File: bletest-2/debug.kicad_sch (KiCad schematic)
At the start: 2 parts, among them J3 Conn_ARM_JTAG_SWD_10

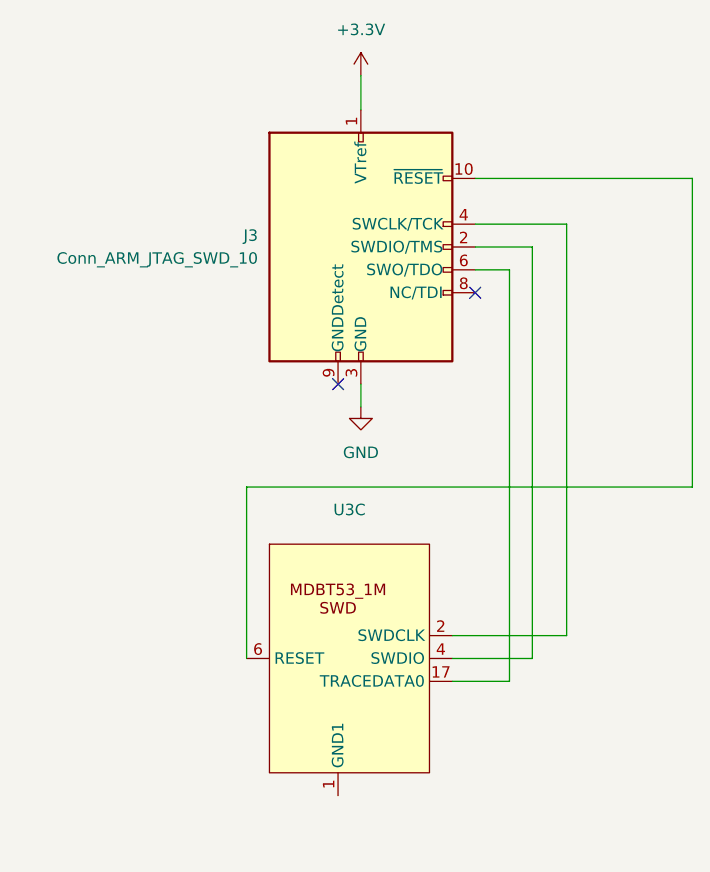
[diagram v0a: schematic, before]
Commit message: Full routing done
There are still a bunch of ERC violations.
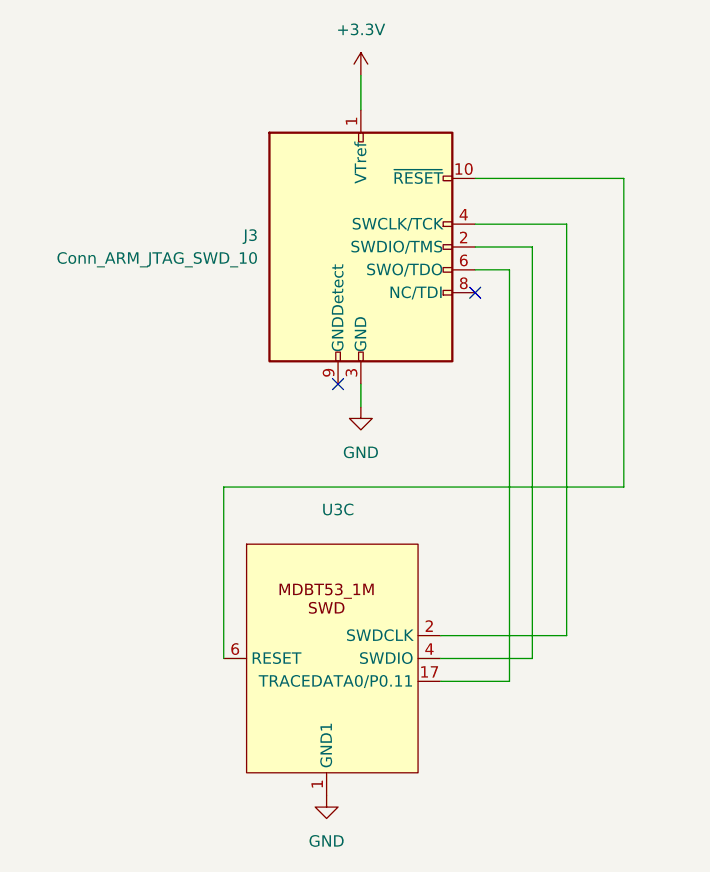
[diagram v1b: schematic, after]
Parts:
- J3: symbol Connector:Conn_ARM_JTAG_SWD_10 -> David Brown Keyboard Parts:Conn_ARM_JTAG_SWD_10
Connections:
- net GND: now also U3.1 (GND1)
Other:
- moved on the sheet: U3C
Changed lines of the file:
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@@
 	(wire
 		(pts
-			(xy 106.68 93.98) (xy 106.68 59.69)
+			(xy 99.06 93.98) (xy 99.06 59.69)
 		)
 		(stroke
@@
 	(wire
 		(pts
-			(xy 88.9 113.03) (xy 80.01 113.03)
+			(xy 88.9 113.03) (xy 78.74 113.03)
 		)
 		(stroke
@@
 	(wire
 		(pts
-			(xy 92.71 110.49) (xy 80.01 110.49)
+			(xy 92.71 110.49) (xy 78.74 110.49)
 		)
 		(stroke
@@
 	(wire
 		(pts
-			(xy 57.15 113.03) (xy 57.15 93.98)
+			(xy 54.61 113.03) (xy 54.61 93.98)
 		)
 		(stroke
@@
 	(wire
 		(pts
-			(xy 106.68 59.69) (xy 82.55 59.69)
+			(xy 99.06 59.69) (xy 82.55 59.69)
 		)
 		(stroke
@@
 	(wire
 		(pts
-			(xy 57.15 93.98) (xy 106.68 93.98)
+			(xy 54.61 93.98) (xy 99.06 93.98)
 		)
 		(stroke
@@
 	(wire
 		(pts
-			(xy 86.36 115.57) (xy 80.01 115.57)
+			(xy 86.36 115.57) (xy 78.74 115.57)
 		)
 		(stroke
@@
 	(symbol
 		(lib_id "David Brown Keyboard Parts:MDBT53_1M")
-		(at 67.31 113.03 0)
+		(at 66.04 113.03 0)
 		(unit 3)
 		(exclude_from_sim no)
@@
 		(fields_autoplaced yes)
 		(property "Reference" "U3"
-			(at 68.58 96.52 0)
+			(at 67.31 96.52 0)
 			(effects
 				(font
@@
 		)
 		(property "Value" "~"
-			(at 68.58 99.06 0)
+			(at 67.31 99.06 0)
 			(effects
 				(font
@@
 		)
 		(property "Footprint" "davidb-keyboard-foot:MDBT53_1M"
-			(at 67.31 115.57 0)
+			(at 66.04 115.57 0)
 			(effects
 				(font
@@
 		)
 		(property "Datasheet" ""
-			(at 67.31 115.57 0)
+			(at 66.04 115.57 0)
 			(effects
 				(font
@@
 		)
 		(property "Description" ""
-			(at 67.31 115.57 0)
+			(at 66.04 115.57 0)
 			(effects
 				(font
@@
 		(pin "16"
 		)
-		(pin "21"
-		)
-		(pin "23"
-		)
-		(pin "26"
-		)
 		(pin "27"
 		)
@@
 		(pin "13"
 		)
+		(pin "15"
+		)
+		(pin "18"
+		)
+		(pin "29"
+		)
+		(pin "30"
+		)
+		(pin "32"
+		)
+		(pin "44"
+		)
+		(pin "46"
+		)
+		(pin "48"
+		)
+		(pin "55"
+		)
+		(pin "59"
+		)
+		(pin "63"
+		)
+		(pin "64"
+		)
+		(pin "24"
+		)
+		(pin "54"
+		)
+		(pin "61"
+		)
+		(pin "41"
+		)
+		(pin "58"
+		)
+		(pin "50"
+		)
+		(pin "40"
+		)
+		(pin "42"
+		)
+		(pin "52"
+		)
+		(pin "38"
+		)
 		(pin "14"
-		)
-		(pin "15"
-		)
-		(pin "16"
-		)
-		(pin "17"
-		)
-		(pin "18"
-		)
-		(pin "27"
-		)
-		(pin "28"
-		)
-		(pin "29"
-		)
-		(pin "30"
-		)
-		(pin "32"
-		)
-		(pin "39"
-		)
-		(pin "5"
-		)
-		(pin "60"
-		)
-		(pin "7"
-		)
-		(pin "9"
-		)
-		(pin "44"
-		)
-		(pin "46"
-		)
-		(pin "48"
-		)
-		(pin "55"
-		)
-		(pin "59"
-		)
-		(pin "63"
-		)
-		(pin "64"
-		)
-		(pin "20"
-		)
-		(pin "35"
-		)
-		(pin "37"
-		)
-		(pin "24"
-		)
-		(pin "54"
-		)
-		(pin "61"
-		)
-		(pin "41"
-		)
-		(pin "58"
-		)
-		(pin "50"
-		)
-		(pin "40"
-		)
-		(pin "42"
-		)
-		(pin "52"
-		)
-		(pin "38"
 		)
 		(instances
@@
 	)
 	(symbol
-		(lib_id "Connector:Conn_ARM_JTAG_SWD_10")
+		(lib_id "power:GND")
+		(at 66.04 128.27 0)
+		(unit 1)
+		(exclude_from_sim no)
+		(in_bom yes)
+		(on_board yes)
+		(dnp no)
+		(fields_autoplaced yes)
+		(property "Reference" "#PWR036"
+			(at 66.04 134.62 0)
+			(effects
+				(font
+					(size 1.27 1.27)
+				)
+				(hide yes)
+			)
+		)
+		(property "Value" "GND"
+			(at 66.04 133.35 0)
+			(effects
+				(font
+					(size 1.27 1.27)
+				)
+			)
+		)
+		(property "Footprint" ""
+			(at 66.04 128.27 0)
+			(effects
+				(font
+					(size 1.27 1.27)
+				)
+				(hide yes)
+			)
+		)
+		(property "Datasheet" ""
+			(at 66.04 128.27 0)
+			(effects
+				(font
+					(size 1.27 1.27)
+				)
+				(hide yes)
+			)
+		)
+		(property "Description" "Power symbol creates a global label with name \"GND\" , ground"
+			(at 66.04 128.27 0)
+			(effects
+				(font
+					(size 1.27 1.27)
+				)
+				(hide yes)
+			)
+		)
+		(pin "1"
+		)
+		(instances
+			(project "bletest-2"
+				(path "/8765e634-cc5d-4e93-a9fe-a7a0a02791b6/0b5cb191-5c5b-487f-a8e4-3883104bc485"
+					(reference "#PWR036")
+					(unit 1)
+				)
+			)
+		)
+	)
+	(symbol
+		(lib_id "David Brown Keyboard Parts:Conn_ARM_JTAG_SWD_10")
 		(at 69.85 67.31 0)
 		(unit 1)

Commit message: Rev A of bletest
Finish cleanup, and remove last remaining violations.

There are a handful of silkscreen overlaps with explicit exclusions.
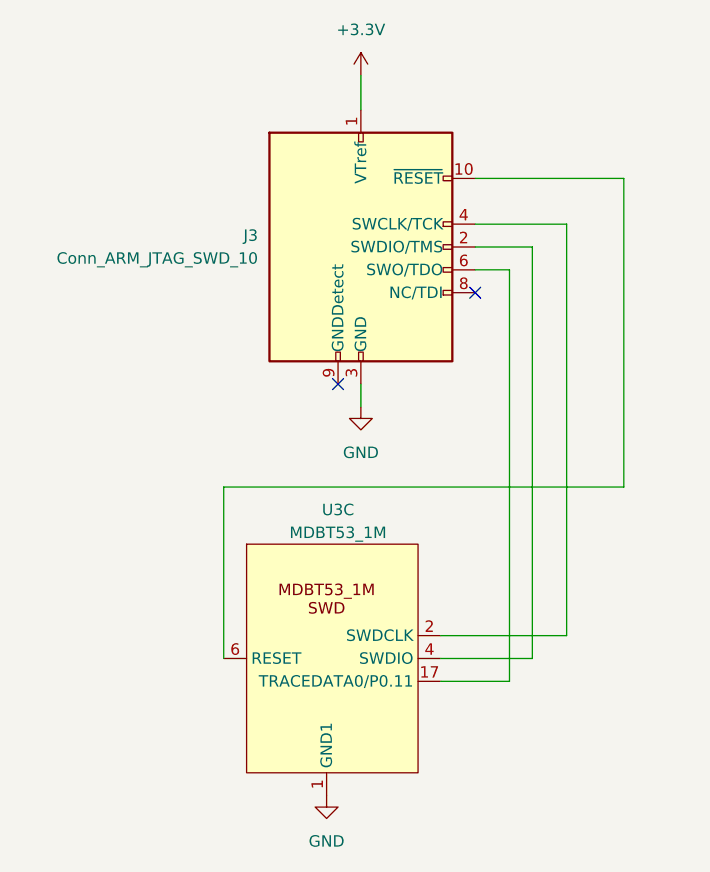
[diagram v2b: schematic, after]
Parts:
- U3: value ~ -> MDBT53_1M
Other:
- company: (none) -> David Brown
- title: (none) -> BLETEXT-2
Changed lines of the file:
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@@
 	(generator "eeschema")
 	(generator_version "8.0")
-	(paper "A4")
+	(paper "A")
+	(title_block
+		(title "BLETEXT-2")
+		(date "2024-12-07")
+		(rev "REVA")
+		(company "David Brown")
+	)
 	(no_connect
 		(at 67.31 82.55)
@@
 			)
 		)
-		(property "Value" "~"
+		(property "Value" "MDBT53_1M"
 			(at 67.31 99.06 0)
 			(effects
@@
 			)
 		)
-		(property "Datasheet" ""
+		(property "Datasheet" "https://www.amazon.com/dp/B0B4BC8Z1V"
 			(at 66.04 115.57 0)
 			(effects
@@
 			)
 		)
-		(property "Datasheet" "http://infocenter.arm.com/help/topic/com.arm.doc.ddi0314h/DDI0314H_coresight_components_trm.pdf"
+		(property "Datasheet" "https://www.digikey.com/en/products/detail/adafruit-industries-llc/4048/9843412"
 			(at 60.96 99.06 90)
 			(effects
